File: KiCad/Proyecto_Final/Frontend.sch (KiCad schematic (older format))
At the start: 68 parts

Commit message: Esquematico terminado con test points.
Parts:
- added C?: 33pF, symbol Device:C
- added C?: 100pF, symbol Device:C
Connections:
- net GND: now also C?.2
- net MIX_CLK: now also C?.1; no longer U?.10 (REF_IN)
- new net REF_IN: C?.1, C?.2, U?.10 (REF_IN)
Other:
- note added: "Divisor capacitivo, 3.3Vpp -> 0.8Vpp"
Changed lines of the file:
@@
 $EndComp
 Text GLabel 6700 5100 3    50   Input ~ 0
-MIX_CLK
+REF_IN
 $Comp
 L Device:R R?
@@
 Wire Wire Line
 	9000 2300 8250 2300
+Text GLabel 9950 4750 0    50   Input ~ 0
+MIX_CLK
+Text GLabel 10350 5200 2    50   Input ~ 0
+REF_IN
+$Comp
+L Device:C C?
+U 1 1 60793144
+P 10150 5450
+F 0 "C?" H 10265 5496 50  0000 L CNN
+F 1 "100pF" H 10265 5405 50  0000 L CNN
+F 2 "" H 10188 5300 50  0001 C CNN
+F 3 "~" H 10150 5450 50  0001 C CNN
+	1    10150 5450
+	1    0    0    -1
+$EndComp
+Wire Wire Line
+	9950 4750 10150 4750
+Wire Wire Line
+	10150 4750 10150 4800
+$Comp
+L Device:C C?
+U 1 1 60792BA4
+P 10150 4950
+F 0 "C?" H 10265 4996 50  0000 L CNN
+F 1 "33pF" H 10265 4905 50  0000 L CNN
+F 2 "" H 10188 4800 50  0001 C CNN
+F 3 "~" H 10150 4950 50  0001 C CNN
+	1    10150 4950
+	1    0    0    -1
+$EndComp
+Wire Wire Line
+	10150 5300 10150 5200
+$Comp
+L power:GND #PWR?
+U 1 1 607A55DE
+P 10150 5600
+F 0 "#PWR?" H 10150 5350 50  0001 C CNN
+F 1 "GND" H 10155 5427 50  0000 C CNN
+F 2 "" H 10150 5600 50  0001 C CNN
+F 3 "" H 10150 5600 50  0001 C CNN
+	1    10150 5600
+	1    0    0    -1
+$EndComp
+Wire Wire Line
+	10350 5200 10150 5200
+Connection ~ 10150 5200
+Wire Wire Line
+	10150 5200 10150 5100
+Wire Notes Line
+	9550 4650 10700 4650
+Wire Notes Line
+	10700 4650 10700 5900
+Wire Notes Line
+	10700 5900 9550 5900
+Wire Notes Line
+	9550 5900 9550 4650
+Text Notes 9550 4600 0    50   ~ 0
+Divisor capacitivo, 3.3Vpp -> 0.8Vpp
 $EndSCHEMATC

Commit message: Empezando con el pcb, loquita.
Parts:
- C1, C10, C11, C12, C13, C14, C15, C16, C17, C18, C2, C20, C21, C22, C23, C24, C25, C26, C27, C28, C29, C3, C30, C31, C32, C33, C35, C36, C37, C38, C39, C4, C40, C41, C42, C43, C44, C45, C46, C47, C48, C5, C6, C7, C8, C9: renamed from C?; footprint (none) -> Capacitor_SMD:C_0402_1005Metric
- C19: renamed from C?; footprint (none) -> Capacitor_SMD:C_0201_0603Metric
- J1: renamed from J?; footprint Connector_Coaxial:SMA_Molex_73251-2120_EdgeMount_Horizontal -> Tesis2020-21:RFSOLUTIONS_CON-SMA-EDGE-S
- L1, L2: renamed from L?; footprint (none) -> Inductor_SMD:L_1210_3225Metric
- Q1: renamed from Q?; footprint SOT95P237X112-3N -> SamacSys_Parts:SOT95P237X112-3N
- R1, R2, R3, R4, R5, R6: renamed from R?; footprint (none) -> Resistor_SMD:R_0402_1005Metric
- T1, T2: renamed from T?; footprint B0310J50100AHF -> SamacSys_Parts:B0310J50100AHF
- gave numbers to parts that had none: 11

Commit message: Empezado PCB.
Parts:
- L1, L2: footprint Inductor_SMD:L_1210_3225Metric -> Inductor_SMD:L_0805_2012Metric
- U1, U3, U4, U5, U6, U7: footprint (none) -> gsg-modules:SKY13351-378LF
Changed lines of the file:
@@
 F 0 "L1" H 7000 1750 50  0000 R CNN
 F 1 "10uH" H 7000 1650 50  0000 R CNN
-F 2 "Inductor_SMD:L_1210_3225Metric" H 7000 1700 50  0001 C CNN
+F 2 "Inductor_SMD:L_0805_2012Metric" H 7000 1700 50  0001 C CNN
 F 3 "~" H 7000 1700 50  0001 C CNN
 	1    7000 1700
@@
 F 0 "L2" H 7153 1746 50  0000 L CNN
 F 1 "10uH" H 7153 1655 50  0000 L CNN
-F 2 "Inductor_SMD:L_1210_3225Metric" H 7100 1700 50  0001 C CNN
+F 2 "Inductor_SMD:L_0805_2012Metric" H 7100 1700 50  0001 C CNN
 F 3 "~" H 7100 1700 50  0001 C CNN
 	1    7100 1700
@@
 F 0 "U5" H 5150 8787 60  0000 C CNN
 F 1 "SKY13351" H 5150 8681 60  0000 C CNN
-F 2 "" H 5150 8350 60  0001 C CNN
+F 2 "gsg-modules:SKY13351-378LF" H 5150 8350 60  0001 C CNN
 F 3 "" H 5150 8350 60  0000 C CNN
 	1    5150 8350
@@
 F 0 "U6" H 9100 8787 60  0000 C CNN
 F 1 "SKY13351" H 9100 8681 60  0000 C CNN
-F 2 "" H 9100 8350 60  0001 C CNN
+F 2 "gsg-modules:SKY13351-378LF" H 9100 8350 60  0001 C CNN
 F 3 "" H 9100 8350 60  0000 C CNN
 	1    9100 8350
@@
 F 0 "U7" H 10900 8787 60  0000 C CNN
 F 1 "SKY13351" H 10900 8681 60  0000 C CNN
-F 2 "" H 10900 8350 60  0001 C CNN
+F 2 "gsg-modules:SKY13351-378LF" H 10900 8350 60  0001 C CNN
 F 3 "" H 10900 8350 60  0000 C CNN
 	1    10900 8350
@@
 F 0 "U1" H 10350 2837 60  0000 C CNN
 F 1 "SKY13351" H 10350 2731 60  0000 C CNN
-F 2 "" H 10350 2400 60  0001 C CNN
+F 2 "gsg-modules:SKY13351-378LF" H 10350 2400 60  0001 C CNN
 F 3 "" H 10350 2400 60  0000 C CNN
 	1    10350 2400
@@
 F 0 "U3" H 2000 8787 60  0000 C CNN
 F 1 "SKY13351" H 2000 8681 60  0000 C CNN
-F 2 "" H 2000 8350 60  0001 C CNN
+F 2 "gsg-modules:SKY13351-378LF" H 2000 8350 60  0001 C CNN
 F 3 "" H 2000 8350 60  0000 C CNN
 	1    2000 8350
@@
 F 0 "U4" H 3400 8787 60  0000 C CNN
 F 1 "SKY13351" H 3400 8681 60  0000 C CNN
-F 2 "" H 3400 8350 60  0001 C CNN
+F 2 "gsg-modules:SKY13351-378LF" H 3400 8350 60  0001 C CNN
 F 3 "" H 3400 8350 60  0000 C CNN
 	1    3400 8350

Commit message: Avance PCB.
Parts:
- added R2: 10k, Resistor_SMD:R_0402_1005Metric, symbol Device:R
- renumbered C14 to C13, C15 to C14, C16 to C15, C17 to C16, C13 to C17, R2 to R3, R3 to R4, R4 to R5, R5 to R6, R6 to R7
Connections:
- net +3V3: now also R2.1
- net MIX_IPN: now also T2.3 (BP1); no longer T2.4 (BP2)
- net MIX_IPP: now also T2.4 (BP2); no longer T2.3 (BP1)
- net SPI1_CS0: now also R2.2
- net SWITCH: now also U1.1 (OUT1); no longer U1.3 (OUT2)
- net MIX_OPN: now reaches L2.2, T1.4 (BP2), U2.27 (MIX_OPN)
- net MIX_OPP: now reaches L1.2, T1.3 (BP1), U2.28 (MIX_OPP)
- net at C10.1: now also U1.3 (OUT2); no longer U1.1 (OUT1)
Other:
- moved on the sheet: C10, C13, C14, C15, C17

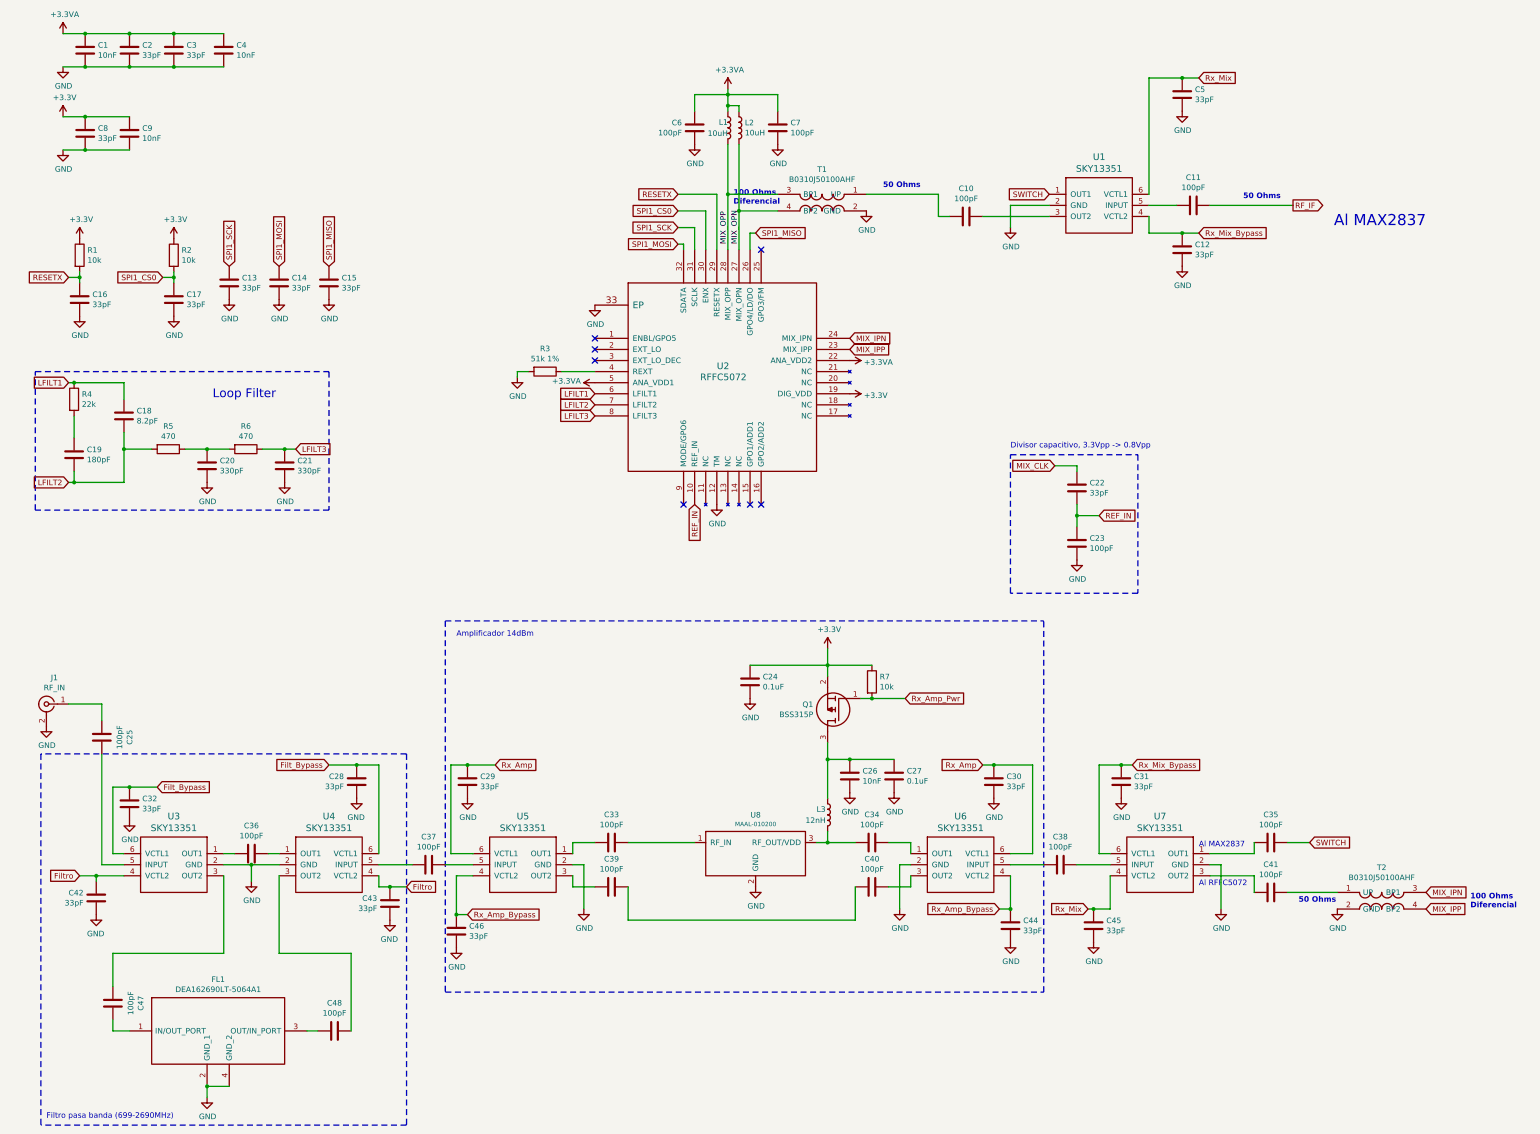
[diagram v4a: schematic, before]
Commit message: PCB Frontend terminado y empezado parte Transceptor.
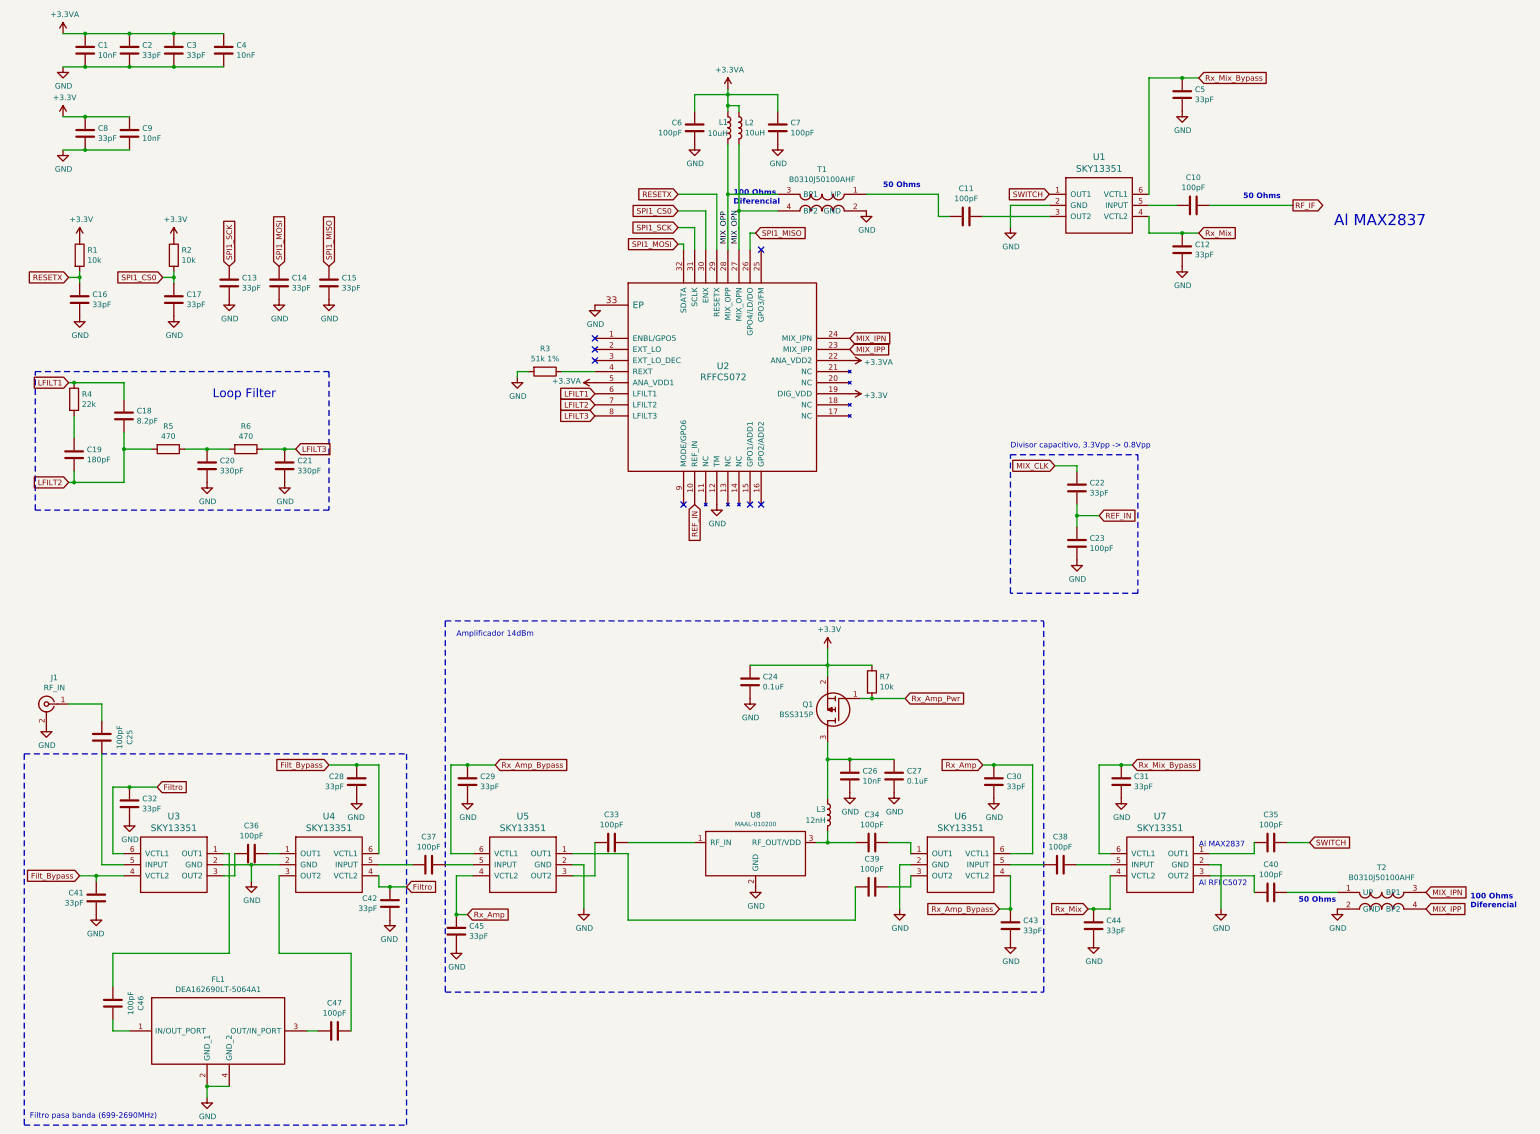
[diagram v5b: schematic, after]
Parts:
- removed C39: 100pF, Capacitor_SMD:C_0402_1005Metric, symbol Device:C
- renumbered C11 to C10, C10 to C11, C40 to C39, C41 to C40, C42 to C41, C43 to C42, C44 to C43, C45 to C44, C46 to C45, C47 to C46, C48 to C47
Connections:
- net Filt_Bypass: now also C41.1, U3.4 (VCTL2); no longer C32.1, U3.6 (VCTL1)
- net Filtro: now also C32.1, U3.6 (VCTL1); no longer C41.1, U3.4 (VCTL2)
- net Rx_Amp: now also C45.1, U5.4 (VCTL2); no longer C29.1, U5.6 (VCTL1)
- net Rx_Amp_Bypass: now also C29.1, U5.6 (VCTL1); no longer C45.1, U5.4 (VCTL2)
- net Rx_Mix: now also C12.1, U1.4 (VCTL2); no longer C5.1, U1.6 (VCTL1)
- net Rx_Mix_Bypass: now also C5.1, U1.6 (VCTL1); no longer C12.1, U1.4 (VCTL2)
- net at U5.1 (OUT1): now also C39.2; no longer C33.2
- net at U5.3 (OUT2): now also C33.2
- net at U3.1 (OUT1): now also C46.2; no longer C36.2
- net at U3.3 (OUT2): now also C36.2; no longer C46.2
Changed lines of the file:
@@
 	4700 8450 4550 8450
 Text GLabel 4900 7450 2    50   Input ~ 0
+Rx_Amp_Bypass
+Text GLabel 4650 8800 2    50   Input ~ 0
 Rx_Amp
-Text GLabel 4650 8800 2    50   Input ~ 0
-Rx_Amp_Bypass
 $Comp
 L Device:C C33
@@
 $EndComp
 $Comp
-L Device:C C39
-U 1 1 601F4A10
-P 5950 8550
-F 0 "C39" V 5698 8550 50  0000 C CNN
-F 1 "100pF" V 5789 8550 50  0000 C CNN
-F 2 "Capacitor_SMD:C_0402_1005Metric" H 5988 8400 50  0001 C CNN
-F 3 "~" H 5950 8550 50  0001 C CNN
-	1    5950 8550
-	0    1    1    0
-$EndComp
-Wire Wire Line
-	5600 8250 5600 8150
-Wire Wire Line
-	5600 8150 5800 8150
-Wire Wire Line
-	5600 8450 5600 8550
-Wire Wire Line
-	5600 8550 5800 8550
-$Comp
 L power:GND #PWR040
 U 1 1 601FAAAB
@@
 $EndComp
 $Comp
-L Device:C C46
+L Device:C C45
 U 1 1 602084F0
 P 4550 8950
-F 0 "C46" H 4665 8996 50  0000 L CNN
+F 0 "C45" H 4665 8996 50  0000 L CNN
 F 1 "33pF" H 4665 8905 50  0000 L CNN
 F 2 "Capacitor_SMD:C_0402_1005Metric" H 4588 8800 50  0001 C CNN
@@
 $EndComp
 $Comp
-L Device:C C40
+L Device:C C39
 U 1 1 60236629
 P 8300 8550
-F 0 "C40" V 8048 8550 50  0000 C CNN
+F 0 "C39" V 8048 8550 50  0000 C CNN
 F 1 "100pF" V 8139 8550 50  0000 C CNN
 F 2 "Capacitor_SMD:C_0402_1005Metric" H 8338 8400 50  0001 C CNN
@@
 Wire Wire Line
 	8650 8550 8450 8550
-Wire Wire Line
-	6100 8550 6100 8850
 Wire Wire Line
 	6100 8850 8150 8850
@@
 Rx_Amp_Bypass
 $Comp
-L Device:C C44
+L Device:C C43
 U 1 1 6024FE9E
 P 9550 8900
-F 0 "C44" H 9665 8946 50  0000 L CNN
+F 0 "C43" H 9665 8946 50  0000 L CNN
 F 1 "33pF" H 9665 8855 50  0000 L CNN
 F 2 "Capacitor_SMD:C_0402_1005Metric" H 9588 8750 50  0001 C CNN
@@
 Rx_Mix
 $Comp
-L Device:C C45
+L Device:C C44
 U 1 1 602653F5
 P 10300 8900
-F 0 "C45" H 10415 8946 50  0000 L CNN
+F 0 "C44" H 10415 8946 50  0000 L CNN
 F 1 "33pF" H 10415 8855 50  0000 L CNN
 F 2 "Capacitor_SMD:C_0402_1005Metric" H 10338 8750 50  0001 C CNN
@@
 $EndComp
 $Comp
-L Device:C C41
+L Device:C C40
 U 1 1 6026BB01
 P 11900 8600
-F 0 "C41" V 11648 8600 50  0000 C CNN
+F 0 "C40" V 11648 8600 50  0000 C CNN
 F 1 "100pF" V 11739 8600 50  0000 C CNN
 F 2 "Capacitor_SMD:C_0402_1005Metric" H 11938 8450 50  0001 C CNN
@@
 $EndComp
 $Comp
-L Device:C C10
+L Device:C C11
 U 1 1 602F6979
 P 9150 2500
-F 0 "C10" V 8898 2500 50  0000 C CNN
+F 0 "C11" V 8898 2500 50  0000 C CNN
 F 1 "100pF" V 8989 2500 50  0000 C CNN
 F 2 "Capacitor_SMD:C_0402_1005Metric" H 9188 2350 50  0001 C CNN
@@
 Wire Wire Line
 	11450 8350 11450 8750
-Text GLabel 11250 1250 2    50   Input ~ 0
+Text GLabel 11250 2650 2    50   Input ~ 0
 Rx_Mix
 $Comp
@@
 	1    0    0    -1
 $EndComp
-Text GLabel 11250 2650 2    50   Input ~ 0
+Text GLabel 11250 1250 2    50   Input ~ 0
 Rx_Mix_Bypass
 Wire Wire Line
@@
 Al MAX2837
 $Comp
-L Device:C C11
+L Device:C C10
 U 1 1 6032B57F
 P 11200 2400
-F 0 "C11" V 10948 2400 50  0000 C CNN
+F 0 "C10" V 10948 2400 50  0000 C CNN
 F 1 "100pF" V 11039 2400 50  0000 C CNN
 F 2 "Capacitor_SMD:C_0402_1005Metric" H 11238 2250 50  0001 C CNN
@@
 $EndComp
 $Comp
-L Device:C C48
+L Device:C C47
 U 1 1 605E6132
 P 3450 9850
-F 0 "C48" V 3198 9850 50  0000 C CNN
+F 0 "C47" V 3198 9850 50  0000 C CNN
 F 1 "100pF" V 3289 9850 50  0000 C CNN
 F 2 "Capacitor_SMD:C_0402_1005Metric" H 3488 9700 50  0001 C CNN
@@
 $EndComp
 $Comp
-L Device:C C47
+L Device:C C46
 U 1 1 605E65E1
 P 1450 9600
-F 0 "C47" V 1198 9600 50  0000 C CNN
+F 0 "C46" V 1198 9600 50  0000 C CNN
 F 1 "100pF" V 1289 9600 50  0000 C CNN
 F 2 "Capacitor_SMD:C_0402_1005Metric" H 1488 9450 50  0001 C CNN
@@
 Wire Wire Line
 	1450 9450 1450 9150
-Wire Wire Line
-	2450 9150 2450 8450
 $Comp
 L Device:C C36
@@
 $EndComp
 Wire Wire Line
-	2550 8250 2450 8250
-Wire Wire Line
 	2850 8250 2950 8250
 $Comp
@@
 Filtro
 $Comp
-L Device:C C43
+L Device:C C42
 U 1 1 6063DA2E
 P 3950 8700
-F 0 "C43" H 4065 8746 50  0000 L CNN
+F 0 "C42" H 4065 8746 50  0000 L CNN
 F 1 "33pF" H 4065 8655 50  0000 L CNN
 F 2 "Capacitor_SMD:C_0402_1005Metric" H 3988 8550 50  0001 C CNN
@@
 Text GLabel 3400 7450 0    50   Input ~ 0
 Filt_Bypass
-Text GLabel 1850 7650 2    50   Input ~ 0
+Text GLabel 1150 8450 0    50   Input ~ 0
 Filt_Bypass
 Wire Wire Line
@@
 Wire Wire Line
 	3600 9150 2950 9150
-Wire Wire Line
-	1450 9150 2450 9150
 $Comp
 L Device:C C32
@@
 Connection ~ 4550 8800
 $Comp
-L Device:C C42
+L Device:C C41
 U 1 1 607E4817
 P 1300 8650
-F 0 "C42" H 1415 8696 50  0000 L CNN
+F 0 "C41" H 1415 8696 50  0000 L CNN
 F 1 "33pF" H 1415 8605 50  0000 L CNN
 F 2 "Capacitor_SMD:C_0402_1005Metric" H 1338 8500 50  0001 C CNN
@@
 	-1   0    0    -1
 $EndComp
-Text GLabel 1150 8450 0    50   Input ~ 0
+Text GLabel 1850 7650 2    50   Input ~ 0
 Filtro
 $Comp
@@
 Connection ~ 3650 7450
 Wire Notes Line
-	4100 7350 800  7350
-Wire Notes Line
-	4100 10700 800  10700
-Wire Notes Line
-	800  7350 800  10700
+	650  7350 650  10700
 Wire Notes Line
 	4100 7350 4100 10700
-Text Notes 850  10650 0    50   ~ 0
+Text Notes 700  10650 0    50   ~ 0
 Filtro pasa banda (699-2690MHz)
 Wire Wire Line
@@
 Text Label 7100 2750 1    50   ~ 0
 MIX_OPN
+Wire Wire Line
+	5800 8150 5800 8450
+Wire Wire Line
+	5800 8450 5600 8450
+Wire Wire Line
+	5600 8250 6100 8250
+Wire Wire Line
+	6100 8250 6100 8850
+Wire Wire Line
+	2550 8250 2550 8450
+Wire Wire Line
+	2550 8450 2450 8450
+Wire Wire Line
+	2450 8250 2500 8250
+Wire Wire Line
+	2500 8250 2500 9150
+Wire Wire Line
+	1450 9150 2500 9150
+Wire Notes Line
+	650  7350 4100 7350
+Wire Notes Line
+	650  10700 4100 10700
 $EndSCHEMATC

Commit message: PCB MCU empezado.
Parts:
- C24: value 0.1uF -> 100nF
- C27: value 0.1uF -> 1uF; footprint Capacitor_SMD:C_0402_1005Metric -> Capacitor_SMD:C_0805_2012Metric
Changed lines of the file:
@@
 P 8500 7550
 F 0 "C27" H 8615 7596 50  0000 L CNN
-F 1 "0.1uF" H 8615 7505 50  0000 L CNN
-F 2 "Capacitor_SMD:C_0402_1005Metric" H 8538 7400 50  0001 C CNN
+F 1 "1uF" H 8615 7505 50  0000 L CNN
+F 2 "Capacitor_SMD:C_0805_2012Metric" H 8538 7400 50  0001 C CNN
 F 3 "~" H 8500 7550 50  0001 C CNN
 	1    8500 7550
@@
 P 7200 6700
 F 0 "C24" H 7315 6746 50  0000 L CNN
-F 1 "0.1uF" H 7315 6655 50  0000 L CNN
+F 1 "100nF" H 7315 6655 50  0000 L CNN
 F 2 "Capacitor_SMD:C_0402_1005Metric" H 7238 6550 50  0001 C CNN
 F 3 "~" H 7200 6700 50  0001 C CNN
